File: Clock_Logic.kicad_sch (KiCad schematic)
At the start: 25 parts, among them U3 74LS14, U4 74LS109, U5 74LS10, U6 74LS08, U7 74LS393, U8 74LS20

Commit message: layout started
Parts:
- renumbered C14 to C15, C15 to C16, C16 to C17, C17 to C18, C18 to C19, C19 to C20, C20 to C21, C21 to C22, C22 to C23, C23 to C24, C24 to C25, C25 to C26, C26 to C27, C27 to C28, C28 to C29, C29 to C30, C30 to C31, C31 to C32, C32 to C33

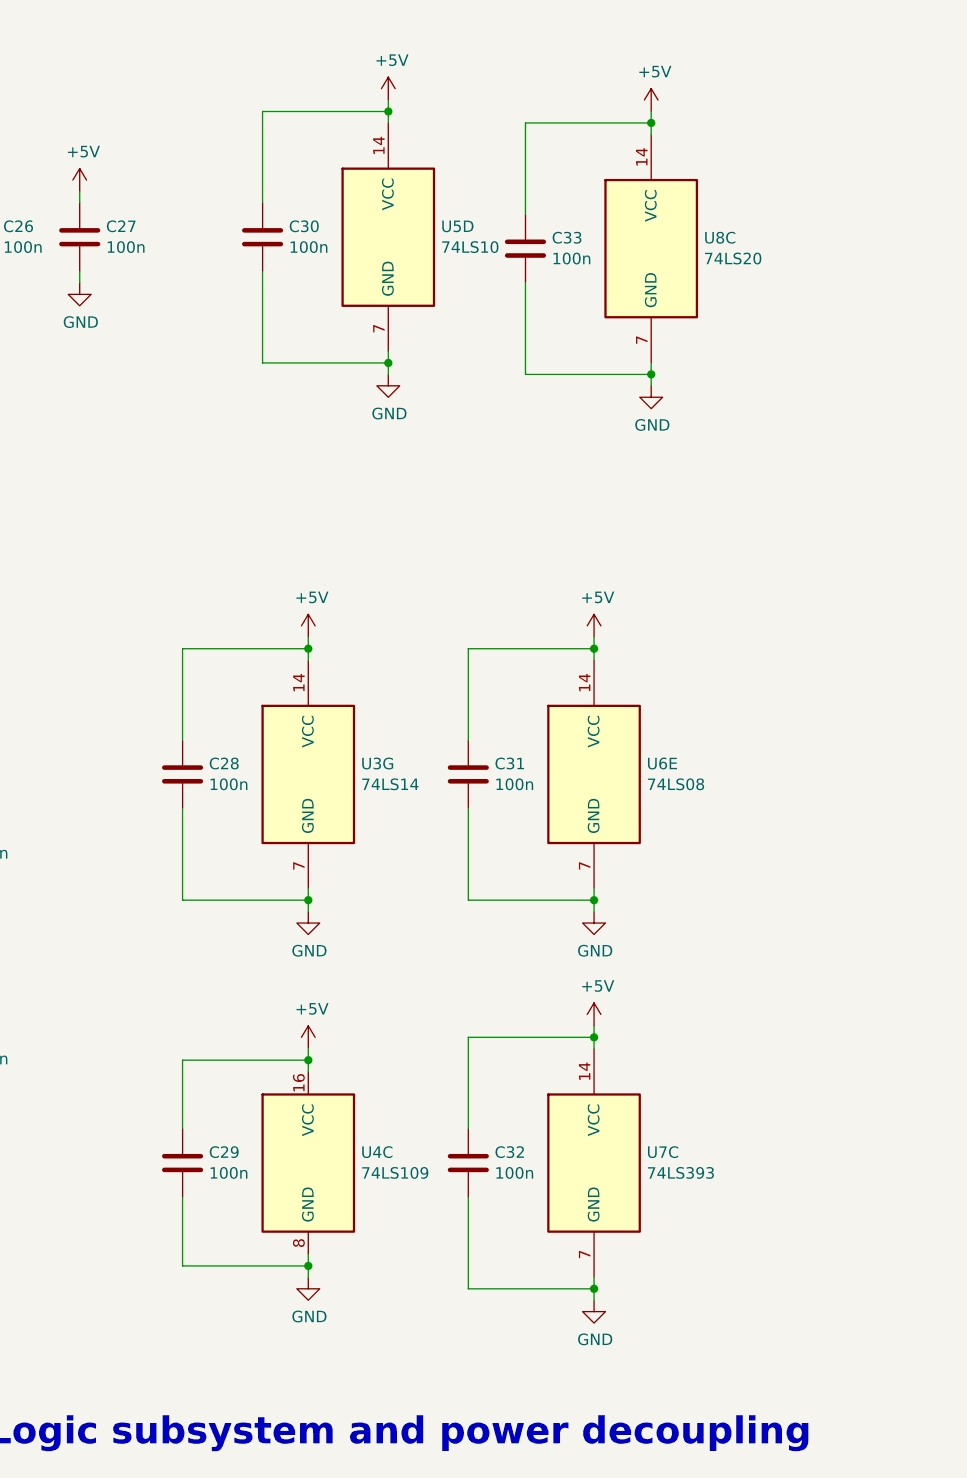
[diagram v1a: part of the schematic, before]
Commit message: Pablo's review, several changes:
Schematic:
- Overall aesthetics
- Added PWR_FLAG to remove ERC errors.
Layout:
- Overall component alignment
- Removed some loops and unnecessary vias.
- Cleaned up vias without ends.
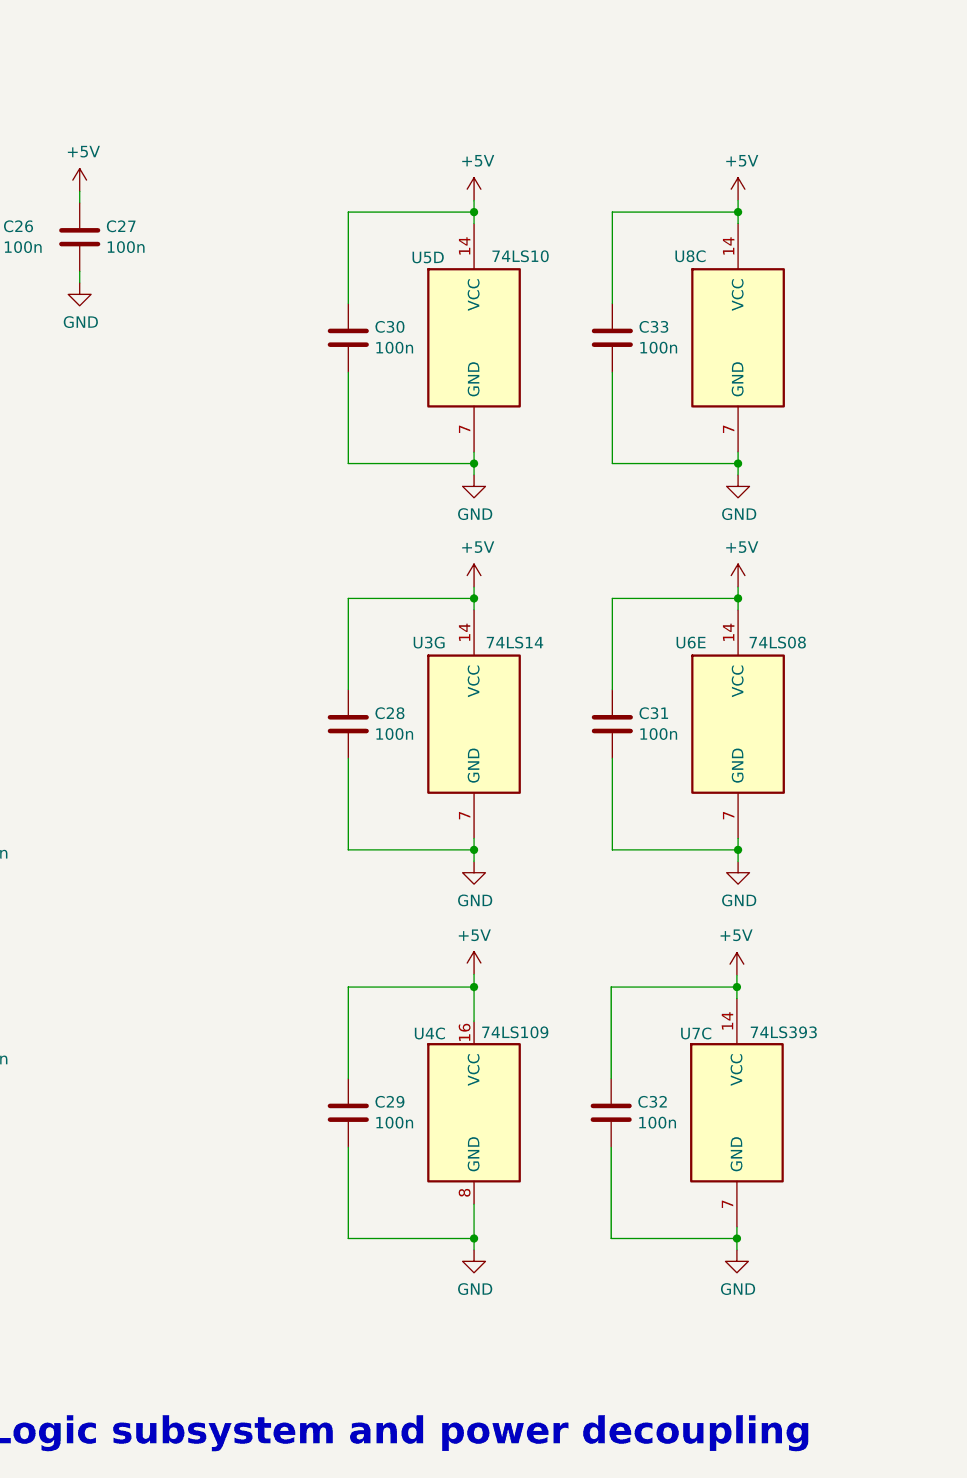
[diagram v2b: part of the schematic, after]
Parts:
- U8: value 74LS20 -> (none); footprint Package_DIP:DIP-14_W7.62mm -> (none)
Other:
- moved on the sheet: C28, C29, C30, C31, C32, C33, U3G, U4C, U5D, U6E, U7C, U8C

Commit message: WIP
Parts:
- U8: value (none) -> 74LS20; footprint (none) -> Package_DIP:DIP-14_W7.62mm
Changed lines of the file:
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@@
       (effects (font (size 1.27 1.27)) (justify left))
     )
-    (property "Value" "" (id 1) (at 264.033 41.529 0)
+    (property "Value" "74LS20" (id 1) (at 264.033 41.529 0)
       (effects (font (size 1.27 1.27)) (justify left))
     )
-    (property "Footprint" "" (id 2) (at 262.382 50.546 0)
+    (property "Footprint" "Package_DIP:DIP-14_W7.62mm" (id 2) (at 262.382 50.546 0)
       (effects (font (size 1.27 1.27)) hide)
     )
